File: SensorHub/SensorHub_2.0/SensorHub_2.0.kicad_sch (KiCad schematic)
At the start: 58 parts, among them J1 Conn_01x02, J4 USB_C_Receptacle, P1 BM46B-12DP-0.35V_53_, P2 BM46B-12DP-0.35V_53_, U1 R7FA4E2B93CFM#AA0, U2 MYRGM080200C41RA, U3 TJA1051TK-3, U4 BMI270, U5 ASCODV-24.000MHZ-LR-T3

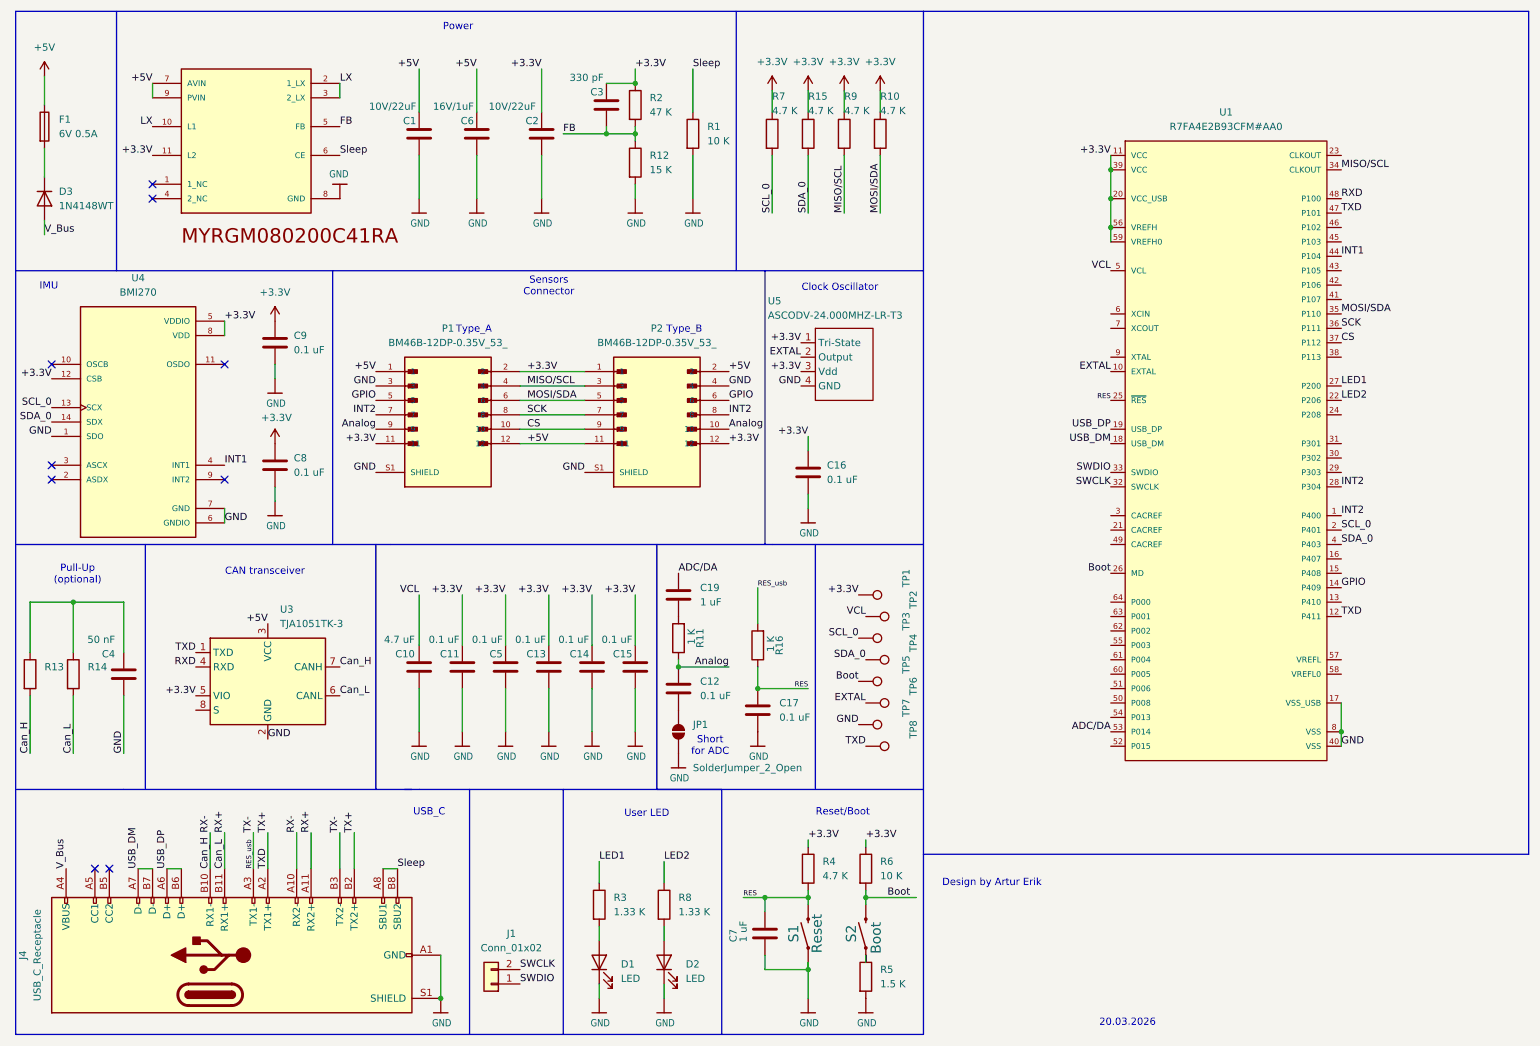
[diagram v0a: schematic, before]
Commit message: New hierarchy
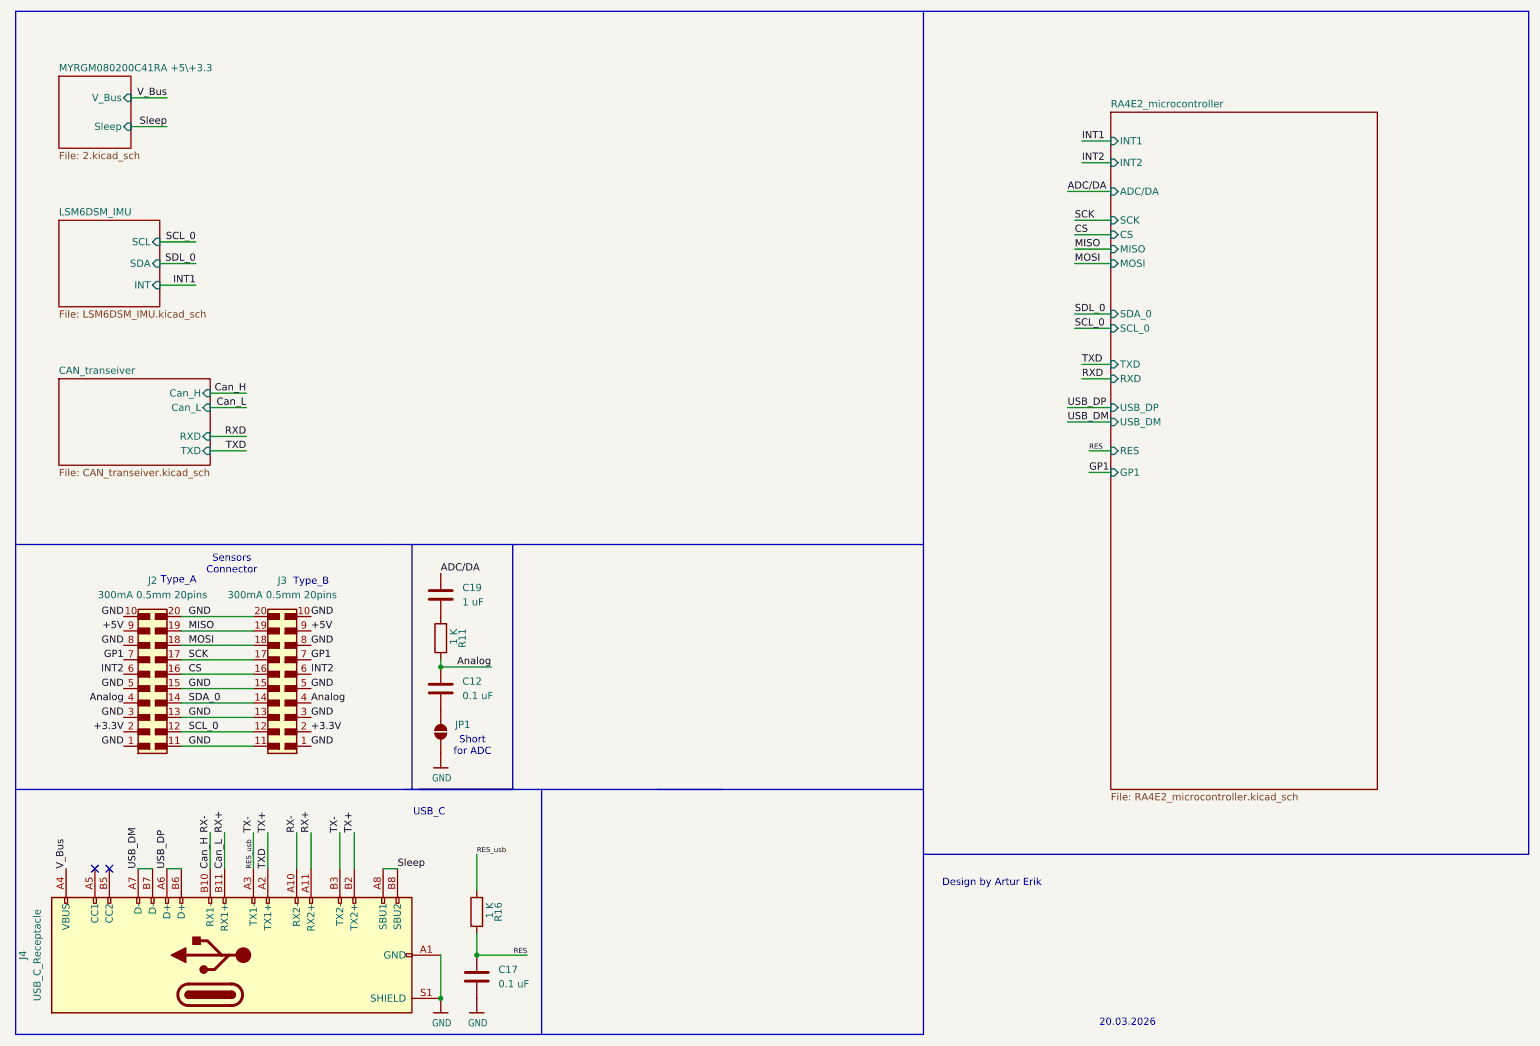
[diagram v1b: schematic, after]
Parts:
- removed C1, C2: 10V/22uF, Capacitor_SMD:C_0603_1608Metric, symbol Device:C
- removed C10: 4.7 uF, Capacitor_SMD:C_0603_1608Metric, symbol Device:C
- removed C11, C13, C14, C15, C16, C5, C8, C9: 0.1 uF, Capacitor_SMD:C_0603_1608Metric, symbol Device:C
- removed C3: 330 pF, Capacitor_SMD:C_0603_1608Metric, symbol Device:C
- removed C4: 50 nF, Capacitor_SMD:C_0603_1608Metric, symbol Device:C
- removed C6: 16V/1uF, Capacitor_SMD:C_0603_1608Metric, symbol Device:C
- removed C7: 1 uF, Capacitor_SMD:C_0603_1608Metric, symbol Device:C
- removed D1, D2: LED, LED_SMD:LED_0402_1005Metric, symbol Device:LED
- removed D3: 1N4148WT, Diode_SMD:D_SOD-523, symbol Diode:1N4148WT
- removed F1: 6V 0.5A, Fuse:Fuse_1206_3216Metric_Pad1.42x1.75mm_HandSolder, symbol Device:Fuse
- removed J1: Conn_01x02, Connector_PinSocket_1.00mm:PinSocket_1x02_P1.00mm_Vertical, symbol Connector_Generic:Conn_01x02
- removed P1, P2: BM46B-12DP-0.35V_53_, BM46B-12DP-0.35V_53_:HRS_BM46B-12DP-0.35V_53_, symbol BM46B-12DP-0.35V_53_:BM46B-12DP-0.35V_53_
- removed R1, R6: 10 K, Resistor_SMD:R_0201_0603Metric, symbol Device:R
- removed R10, R15, R4, R7, R9: 4.7 K, Resistor_SMD:R_0201_0603Metric, symbol Device:R
- removed R12: 15 K, Resistor_SMD:R_0201_0603Metric, symbol Device:R
- removed R13, R14: ~, Resistor_SMD:R_0201_0603Metric, symbol Device:R
- removed R2: 47 K, Resistor_SMD:R_0201_0603Metric, symbol Device:R
- removed R3, R8: 1.33 K, Resistor_SMD:R_0201_0603Metric, symbol Device:R
- removed R5: 1.5 K, Resistor_SMD:R_0201_0603Metric, symbol Device:R
- removed S1: Reset, Library:Button_Mini_2.5x1.7mm, symbol SensorHub MicroMod Carrier v1.1.0b-eagle-import:MOMENTARY-SWITCH-SPST-SMD-5.2-T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
- removed S2: Boot, Library:Button_Mini_2.5x1.7mm, symbol SensorHub MicroMod Carrier v1.1.0b-eagle-import:MOMENTARY-SWITCH-SPST-SMD-5.2-T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
- removed TP1, TP2, TP3, TP4, TP5, TP6, TP7, TP8: TestPoint, TestPoint:TestPoint_THTPad_D1.0mm_Drill0.5mm, symbol Connector:TestPoint
- removed U1: R7FA4E2B93CFM#AA0, eec:Renesas-PLQP0064KB-C-0-0-IPC_A, symbol eec:R7FA4E2B93CFM#AA0
- removed U2: MYRGM080200C41RA, MYRGM080200C41RA:MURATA_MYRGM080200C41RA_0, symbol MYRGM080200C41RA:MYRGM080200C41RA
- removed U3: TJA1051TK-3, Package_SON:HVSON-8-1EP_3x3mm_P0.65mm_EP1.6x2.4mm, symbol Interface_CAN_LIN:TJA1051TK-3
- removed U4: BMI270, BMI270:XDCR_BMI270, symbol BMI270:BMI270
- removed U5: ASCODV-24.000MHZ-LR-T3, Library:ASCODV-24.000MHZ-LR-T3, symbol Library:ASCODV-24.000MHZ-LR-T3
- added J2, J3: 658561423020, Connector_SMD_Wurth:J_Wurth_WR-BTB_658561423020, symbol Connector_Wurth_WR-BTB:658561423020
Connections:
- net +3.3V: now also J2.2, J3.2
- net +5V: now also J2.9, J3.9
- net Analog: now also J2.4, J3.4
- net CS: now also J2.16, J3.16
- net GND: now also J2.1, J2.10, J2.11, J2.13, J2.15, J2.20, J2.3, J2.5, J2.8, J3.1, J3.10, J3.11, J3.13, J3.15, J3.20, J3.3, J3.5, J3.8
- net INT2: now also J2.6, J3.6
- net SCK: now also J2.17, J3.17
- net SCL_0: now also J2.12, J3.12
- net SDA_0: now also J2.14, J3.14
- new net GP1: J2.7, J3.7
- new net MISO: J2.19, J3.19
- new net MOSI: J2.18, J3.18
- no-connect marks 9 -> 2
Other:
- added sheet CAN_transeiver (CAN_transeiver.kicad_sch)
- added sheet LSM6DSM_IMU (LSM6DSM_IMU.kicad_sch)
- added sheet MYRGM080200C41RA +5\+3.3 (2.kicad_sch)
- added sheet RA4E2_microcontroller (RA4E2_microcontroller.kicad_sch)
- note removed: "CAN transceiver"
- note removed: "Clock Oscillator"
- note removed: "IMU"
- note removed: "Power"
- note removed: "Pull-Up (optional)"
- note removed: "Reset/Boot"
- note removed: "User LED"
- moved on the sheet: C12, C17, C19, JP1, R11, R16

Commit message: TCAN334
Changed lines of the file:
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@@
 			)
 		)
-		(pin "INT2" input
+		(pin "INT2" bidirectional
 			(at 208.28 41.91 180)
 			(effects
@@
 			)
 		)
-		(pin "INT1" input
+		(pin "INT1" bidirectional
 			(at 208.28 38.1 180)
 			(effects
@@
 			)
 		)
-		(pin "MISO" input
+		(pin "MISO" bidirectional
 			(at 208.28 57.15 180)
 			(effects
@@
 			)
 		)
-		(pin "CS" input
+		(pin "CS" bidirectional
 			(at 208.28 54.61 180)
 			(effects
@@
 			)
 		)
-		(pin "MOSI" input
+		(pin "MOSI" bidirectional
 			(at 208.28 59.69 180)
 			(effects
@@
 			)
 		)
-		(pin "SCK" input
+		(pin "SCK" bidirectional
 			(at 208.28 52.07 180)
 			(effects
@@
 			)
 		)
-		(pin "SDA_0" input
+		(pin "SDA_0" bidirectional
 			(at 208.28 68.58 180)
 			(effects
@@
 			)
 		)
-		(pin "SCL_0" input
+		(pin "SCL_0" bidirectional
 			(at 208.28 71.12 180)
 			(effects
@@
 			)
 		)
-		(pin "TXD" input
+		(pin "TXD" bidirectional
 			(at 208.28 77.47 180)
 			(effects
@@
 			)
 		)
-		(pin "RXD" input
+		(pin "RXD" bidirectional
 			(at 208.28 80.01 180)
 			(effects
@@
 			)
 		)
-		(pin "USB_DP" input
+		(pin "USB_DP" bidirectional
 			(at 208.28 85.09 180)
 			(effects
@@
 			)
 		)
-		(pin "USB_DM" input
+		(pin "USB_DM" bidirectional
 			(at 208.28 87.63 180)
 			(effects
@@
 			)
 		)
-		(pin "ADC{slash}DA" input
+		(pin "ADC{slash}DA" bidirectional
 			(at 208.28 46.99 180)
 			(effects
@@
 			)
 		)
-		(pin "RES" input
+		(pin "RES" bidirectional
 			(at 208.28 92.71 180)
 			(effects
@@
 			)
 		)
-		(pin "GP1" input
+		(pin "GP1" bidirectional
 			(at 208.28 96.52 180)
 			(effects
@@
 			)
 		)
-		(pin "Sleep" input
+		(pin "Sleep" bidirectional
 			(at 35.56 35.56 0)
 			(effects
@@
 			)
 		)
-		(pin "V_Bus" input
+		(pin "V_Bus" bidirectional
 			(at 35.56 30.48 0)
 			(effects
@@
 			)
 		)
-		(pin "Can_H" input
+		(pin "Can_H" bidirectional
 			(at 49.53 82.55 0)
 			(effects
@@
 			)
 		)
-		(pin "Can_L" input
+		(pin "Can_L" bidirectional
 			(at 49.53 85.09 0)
 			(effects
@@
 			)
 		)
-		(pin "RXD" input
+		(pin "RXD" bidirectional
 			(at 49.53 90.17 0)
 			(effects
@@
 			)
 		)
-		(pin "TXD" input
+		(pin "TXD" bidirectional
 			(at 49.53 92.71 0)
 			(effects
@@
 			)
 		)
-		(pin "SCL" input
+		(pin "SCL" bidirectional
 			(at 40.64 55.88 0)
 			(effects
@@
 			)
 		)
-		(pin "SDA" input
+		(pin "SDA" bidirectional
 			(at 40.64 59.69 0)
 			(effects
@@
 			)
 		)
-		(pin "INT" input
+		(pin "INT" bidirectional
 			(at 40.64 63.5 0)
 			(effects

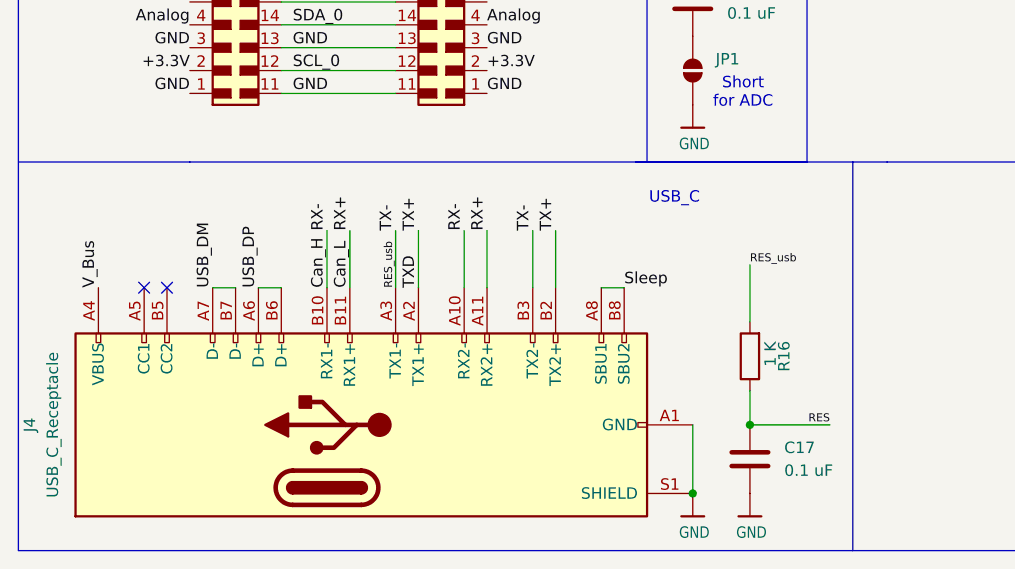
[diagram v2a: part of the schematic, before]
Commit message: 32k oscillator
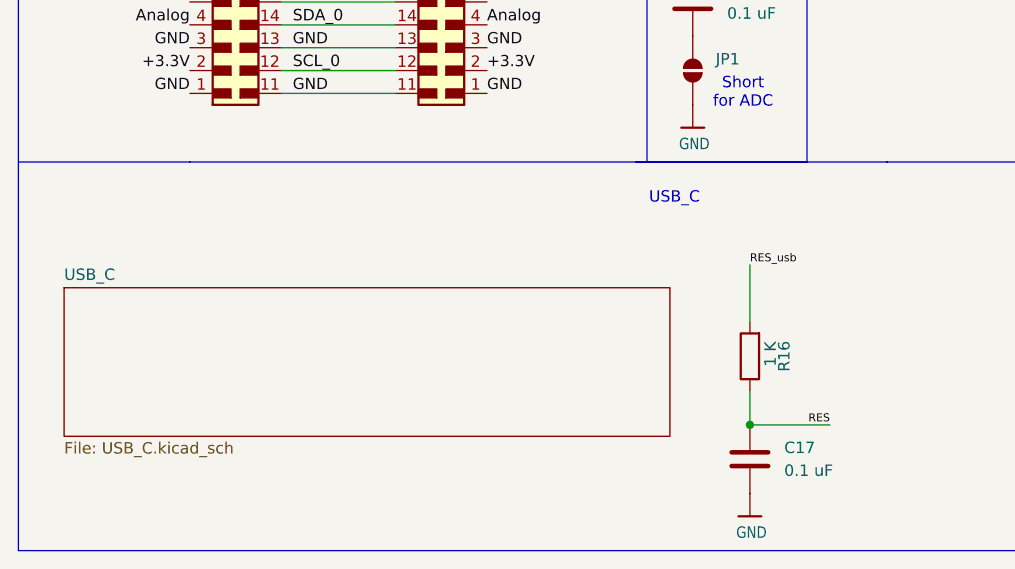
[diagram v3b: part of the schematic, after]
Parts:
- removed J4: USB_C_Receptacle, Connector_USB:USB_C_Receptacle_Molex_105450-0101, symbol Connector:USB_C_Receptacle
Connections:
- no-connect marks 2 -> 0
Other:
- added sheet USB_C (USB_C.kicad_sch)

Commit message: New_USB_2.0
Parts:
- removed C17: 0.1 uF, Capacitor_SMD:C_0603_1608Metric, symbol Device:C
- removed R16: 1 K, Resistor_SMD:R_0201_0603Metric, symbol Device:R
- added TP2, TP7: TestPoint, TestPoint:TestPoint_THTPad_D1.0mm_Drill0.5mm, symbol Connector:TestPoint
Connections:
- new net GP2: TP7.1
- new net GP3: TP2.1
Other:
- sheet USB_C renamed USB_C_2.0+SBUS
- sheet RA4E2_microcontroller ports: added GP2, GP3; removed none
- sheet USB_C_2.0+SBUS: file USB_C.kicad_sch -> USB_C_2.0+SBUS.kicad_sch
- sheet USB_C_2.0+SBUS ports: added Out_1, Out_2, USB_DM, USB_DP, V_Bus; removed none
- note removed: "USB_C"

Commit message: PCB 1st upd
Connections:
- net +3.3V: now also J3.12; no longer J3.2
- net +5V: now also J3.19; no longer J3.9
- net Analog: now also J3.14; no longer J3.4
- net CS: now also J3.6; no longer J3.16
- net GND: now also J3.18; no longer J3.8
- net GP1: now also J3.17; no longer J3.7
- net INT2: now also J3.16; no longer J3.6
- net MISO: now also J3.9; no longer J3.19
- net MOSI: now also J3.8; no longer J3.18
- net SCK: now also J3.7; no longer J3.17
- net SCL_0: now also J3.2; no longer J3.12
- net SDA_0: now also J3.4; no longer J3.14
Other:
- moved on the sheet: J3
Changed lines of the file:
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@@
 		)
 	)
-	(label "SDL_0"
+	(label "SDA_0"
 		(at 201.93 68.58 0)
 		(effects
@@
 	(symbol
 		(lib_id "Connector_Wurth_WR-BTB:658561423020")
-		(at 62.23 133.35 270)
-		(mirror x)
+		(at 62.23 133.35 90)
 		(unit 1)
 		(exclude_from_sim no)
@@
 		(on_board yes)
 		(dnp no)
-		(fields_autoplaced yes)
 		(property "Reference" "J3"
 			(at 62.23 115.57 90)
@@
 		)
 		(property "Value" "658561423020"
-			(at 85.09 120.65 0)
+			(at 39.37 120.65 0)
 			(effects
 				(font
@@
 		)
 		(property "Footprint" "Connector_SMD_Wurth:J_Wurth_WR-BTB_658561423020"
-			(at 82.55 120.65 0)
+			(at 41.91 120.65 0)
 			(effects
 				(font
@@
 		)
 		(property "Datasheet" "https://www.we-online.com/catalog/datasheet/658561423020.pdf?ki"
-			(at 80.01 120.65 0)
+			(at 44.45 120.65 0)
 			(effects
 				(font
@@
 		)
 		(property "Manufacturer" "Wurth Elektronik"
-			(at 77.47 120.65 0)
+			(at 46.99 120.65 0)
 			(effects
 				(font
@@
 		)
 		(property "Manufacturer URL" "https://www.we-online.com"
-			(at 74.93 120.65 0)
+			(at 49.53 120.65 0)
 			(effects
 				(font
@@
 		)
 		(property "Published Date" "20250522"
-			(at 72.39 120.65 0)
+			(at 52.07 120.65 0)
 			(effects
 				(font
@@
 		)
 		(property "Match Code" "WR-BTB"
-			(at 69.85 120.65 0)
+			(at 54.61 120.65 0)
 			(effects
 				(font
@@
 		)
 		(property "Part Number" "658561423020"
-			(at 67.31 120.65 0)
+			(at 57.15 120.65 0)
 			(effects
 				(font
@@
 		)
 		(property "Mounting Technology" "SMT"
-			(at 64.77 120.65 0)
+			(at 59.69 120.65 0)
 			(effects
 				(font
@@
 		)
 		(property "Pitch (mm)" "0.5"
-			(at 59.69 120.65 0)
+			(at 64.77 120.65 0)
 			(effects
 				(font
@@
 		)
 		(property "Pins (pcs)" "20"
-			(at 57.15 120.65 0)
+			(at 67.31 120.65 0)
 			(effects
 				(font
@@
 		)
 		(property "H (mm)" "1.4"
-			(at 54.61 120.65 0)
+			(at 69.85 120.65 0)
 			(effects
 				(font
@@
 		)
 		(property "Gender" "Plug"
-			(at 52.07 120.65 0)
+			(at 72.39 120.65 0)
 			(effects
 				(font
@@
 		)
 		(property "Type" "Vertical"
-			(at 49.53 120.65 0)
+			(at 74.93 120.65 0)
 			(effects
 				(font
@@
 		)
 		(property "gender" "male"
-			(at 46.99 120.65 0)
-			(effects
-				(font
+			(at 77.47 120.65 0)
+			(effects
+				(font

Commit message: PCB upd 2
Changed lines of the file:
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@@
+		)
+	)
+	(label "SCL_0"
+		(at 46.99 55.88 180)
+		(effects
+			(font
+				(size 1.27 1.27)
+			)
+			(justify right bottom)
 		)
 	)
@@
 		)
 	)
-	(label "SCL_0"
-		(at 46.99 55.88 180)
-		(effects
-			(font
-				(size 1.27 1.27)
-			)
-			(justify right bottom)
-		)
-	)
 	(label "GND"
 		(at 45.72 139.7 0)
@@
 		)
 	)
+	(label "SDA_0"
+		(at 46.99 59.69 180)
+		(effects
+			(font
+				(size 1.27 1.27)
+			)
+			(justify right bottom)
+		)
+	)
 	(label "CS"
 		(at 45.72 132.08 0)
@@
 		(effects
 			(font
-				(size 1.27 1.27)
-			)
-			(justify right bottom)
-		)
-	)
-	(label "SDL_0"
-		(at 46.99 59.69 180)
-		(effects
-			(font
